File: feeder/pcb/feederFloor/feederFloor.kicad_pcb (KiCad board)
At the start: 2 copper layers, 13.5 x 40 mm, 6 parts, among them J1 Conn_01x04_Male, J2 Conn_01x10_Female, J3 Conn_01x04_Male

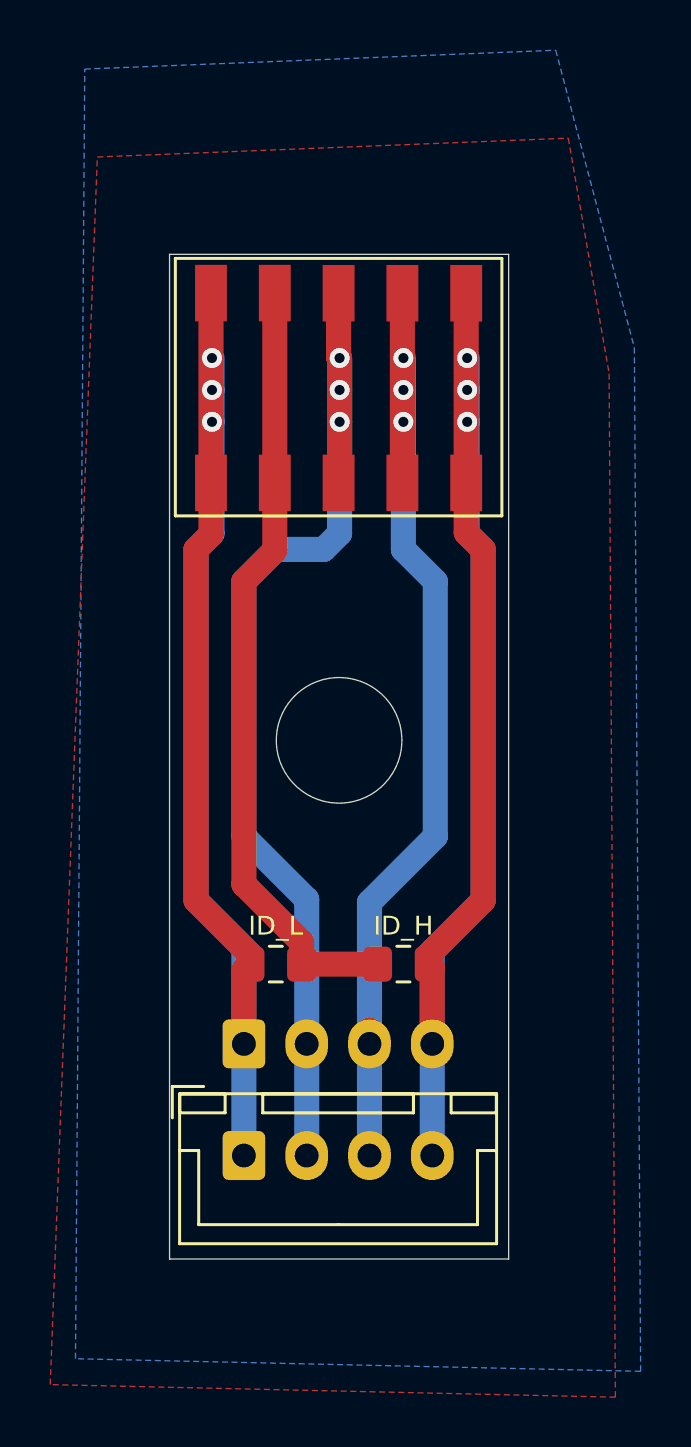
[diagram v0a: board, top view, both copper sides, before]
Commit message: this commit reflects boards ordered for rev04 of the feeder motherboard, rev02 of the indexing wheel, and rev02 of the feeder floor
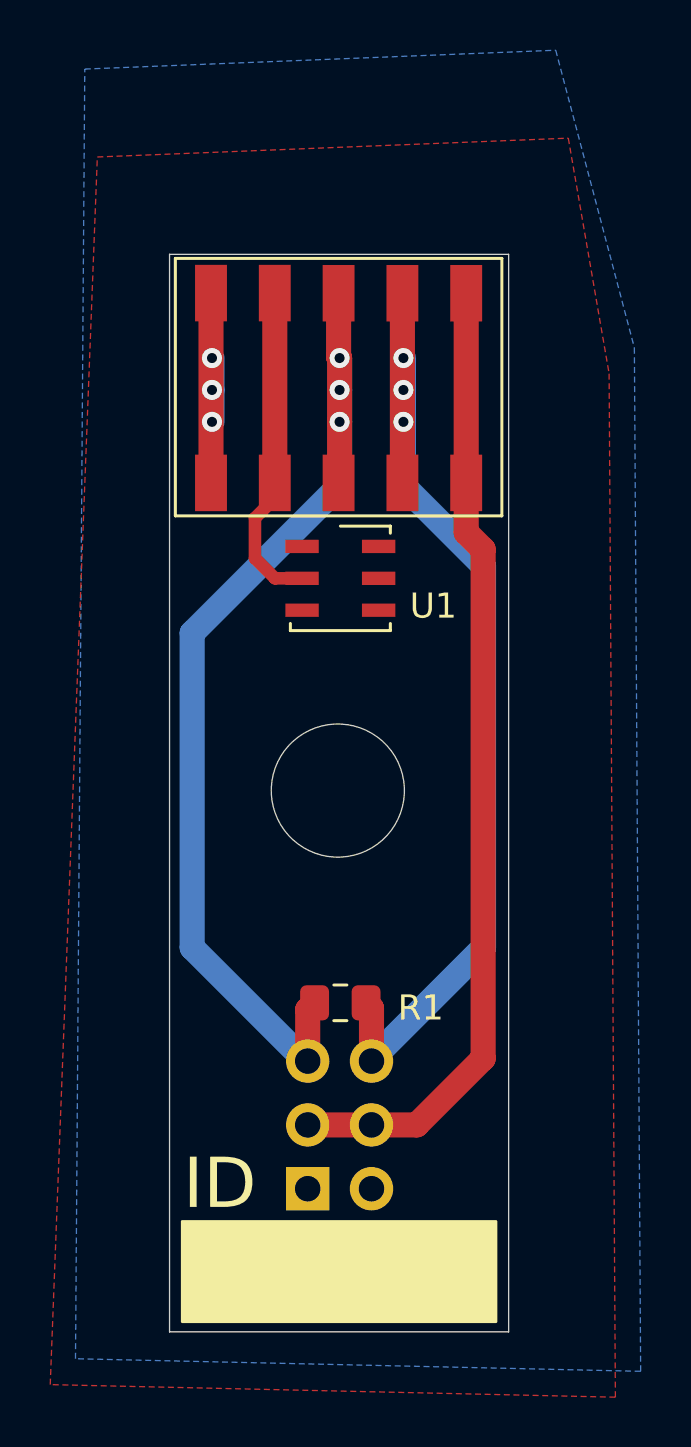
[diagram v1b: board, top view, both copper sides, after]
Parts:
- removed J3: Conn_01x04_Male, Connector_JST:JST_XH_B4B-XH-A_1x04_P2.50mm_Vertical
- removed R2: ID_L, Resistor_SMD:R_0805_2012Metric_Pad1.15x1.40mm_HandSolder
- added H1: MountingHole, MountingHole:MountingHole_5.3mm_M5, F.Cu at (191.7, 41.4)
- added U1: DS2431, Package_SO_J-Lead:TSOC-6_3.76x3.94mm_P1.27mm, F.Cu at (191.8, 32.9)
- J1: value Conn_01x04_Male -> IDC; footprint Connector_JST:JST_XH_B4B-XH-A_1x04_P2.50mm_Vertical -> Connector_IDC:IDC-Header_2x03_P2.54mm_Vertical
- R1: value ID_H -> 220R
- moved J1 6.30 mm to (190.5, 57.2)
- moved G*** 4.70 mm to (191.8, 25.4)
- moved R1 2.94 mm to (191.8, 49.8), turned to 0 degrees
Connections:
- J1 pad 2: B -> GND
- J1 pad 3: A -> VIN
- J1 pad 4: 5V -> VIN
- J2 pad 2: ID -> 1WIRE
- J2 pad 5: 5V -> VIN
- J2 pad 6: 5V -> VIN
- J2 pad 9: ID -> 1WIRE
- R1 pad 1: 5V -> B
- R1 pad 2: ID -> A
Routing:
- net 5V: track 64.0 -> 0.00 mm, vias 3 -> 0
- net GND: track 63.9 -> 10.1 mm
- net VIN: track 0.00 -> 38.8 mm
- net ID: track 31.2 -> 0.00 mm
- net 1WIRE: track 0.00 -> 13.2 mm
- net A: track 42.0 -> 41.1 mm
- net B: track 43.1 -> 42.4 mm
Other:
- board size 13.5 x 40 mm -> 13.5 x 42.9 mm
- board text added: "FEEDER FLOOR REV02"
- board text added: "ID"
- board text removed: "ID_H"
- board text removed: "ID_L"

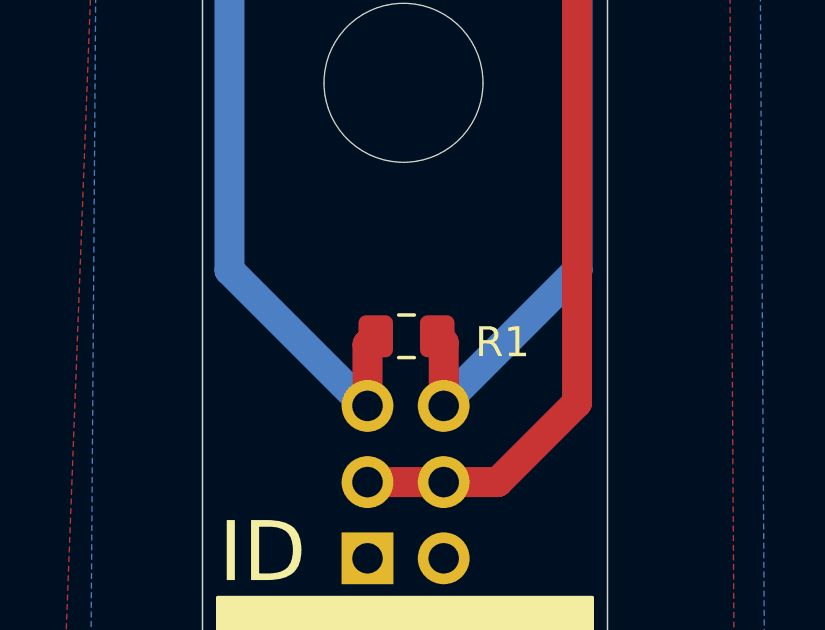
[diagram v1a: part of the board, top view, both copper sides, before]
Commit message: Updating the package of the resistor on the feeder floor.
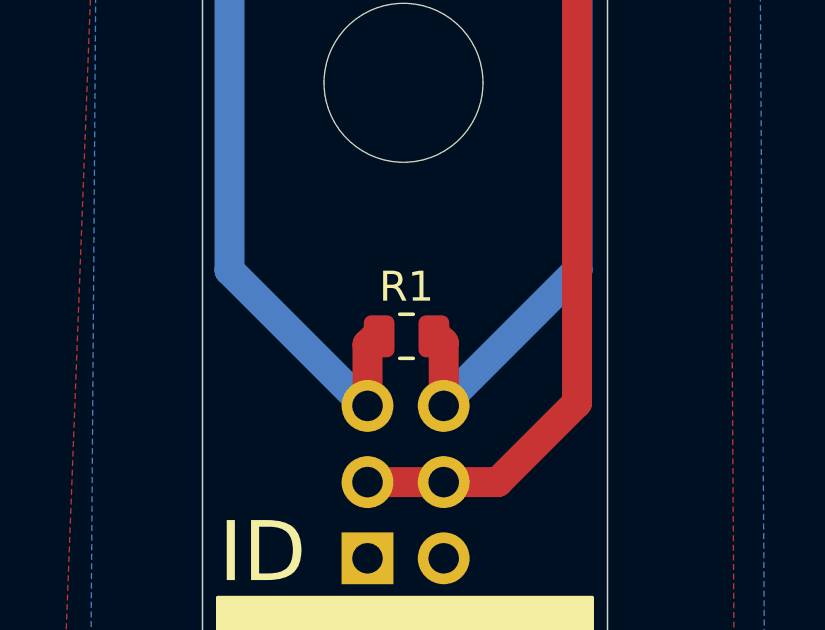
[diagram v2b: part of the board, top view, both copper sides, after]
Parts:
- R1: footprint Resistor_SMD:R_0805_2012Metric_Pad1.15x1.40mm_HandSolder -> Resistor_SMD:R_0805_2012Metric

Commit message: Adding the git hash to the feeder mobo, feeder floor and indexing wheel boards.
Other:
- board text added: "FEEDER FLOOR REV02 <<hash>>"
- board text removed: "FEEDER FLOOR REV02"

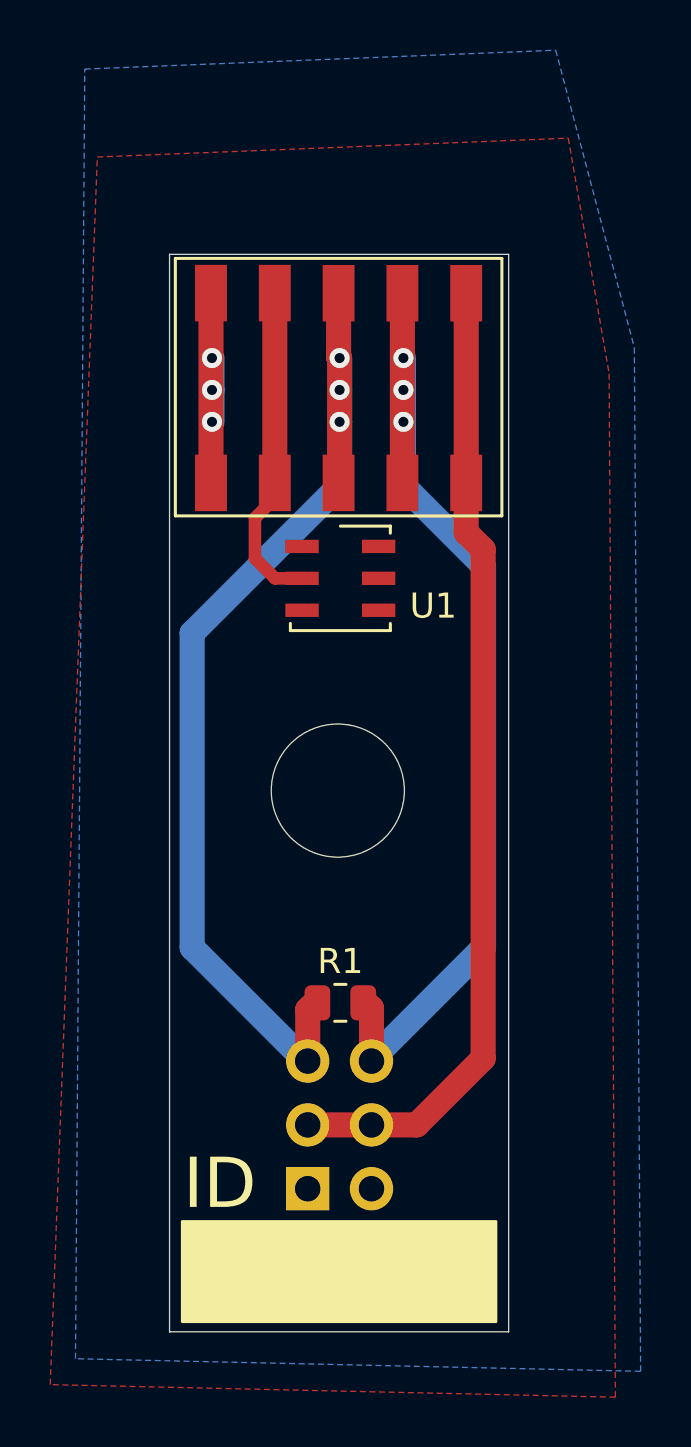
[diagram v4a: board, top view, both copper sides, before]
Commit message: Route bus as diff pairs, pad for screw head and beautify
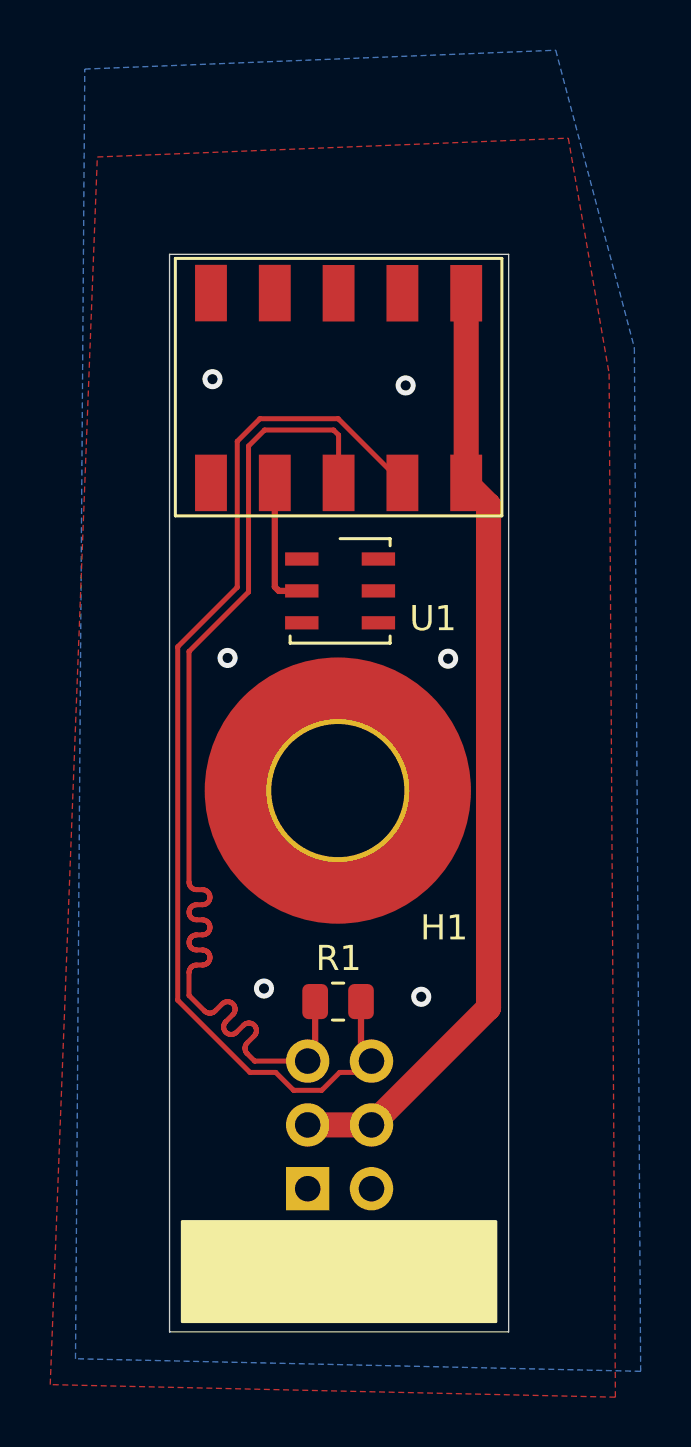
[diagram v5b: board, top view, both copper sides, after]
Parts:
- removed G***: LOGO, index:logo
- H1: footprint MountingHole:MountingHole_5.3mm_M5 -> MountingHole:MountingHole_5.3mm_M5_Pad_TopOnly
- R1: value 220R -> 120R
- moved U1 0.50 mm to (191.8, 33.4)
- moved R1 0.10 mm to (191.7, 49.8)
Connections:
- net A renamed RS-485+
- net B renamed RS-485-
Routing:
- net GND: track 10.1 -> 0.00 mm, vias 3 -> 6
- net 1WIRE: track 13.2 -> 5.28 mm
- net RS-485+: track 41.1 -> 43.5 mm, vias 3 -> 0
- net RS-485-: track 42.4 -> 43.4 mm, vias 3 -> 0
- net VIN: track 38.8 -> 37.9 mm
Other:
- board text removed: "ID"

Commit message: Fix bus wires on feeder floors
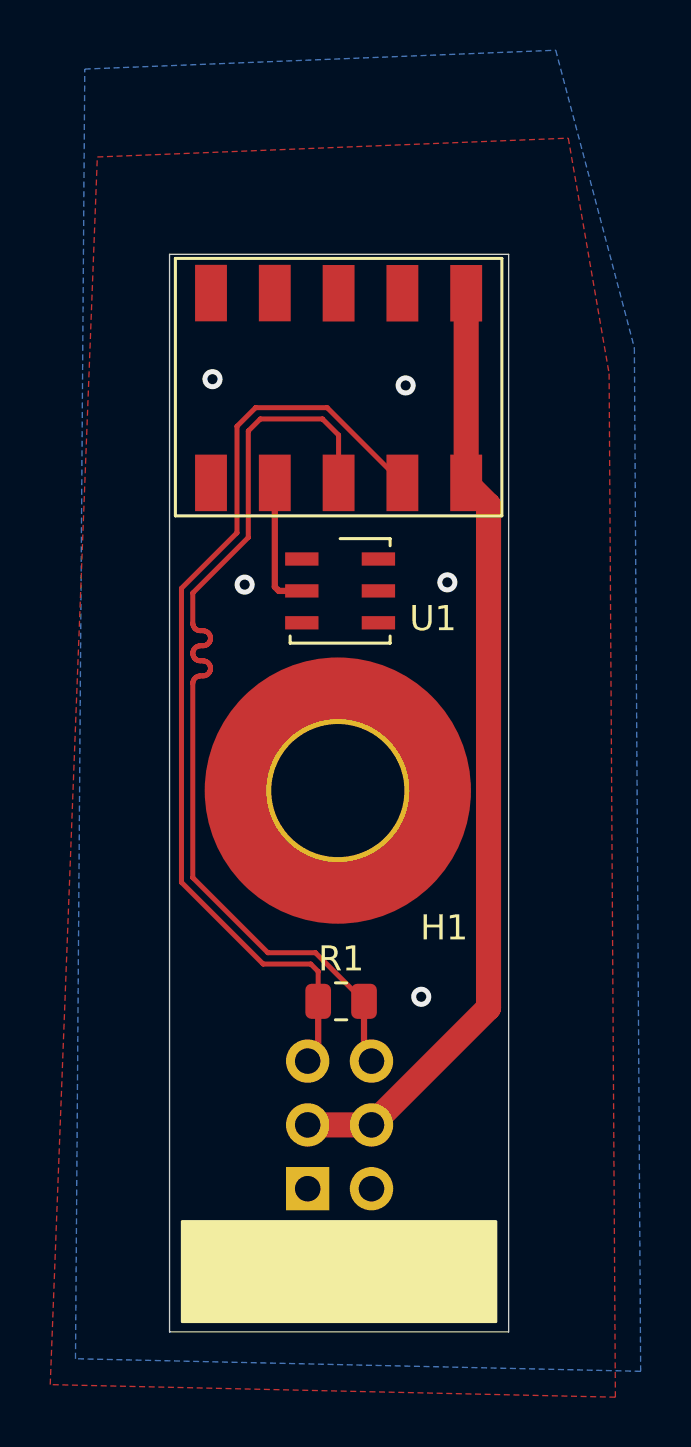
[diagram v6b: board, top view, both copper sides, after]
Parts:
- moved R1 0.12 mm to (191.8, 49.7), turned to 180 degrees
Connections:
- J1 pad 5: RS-485- -> RS-485+
- J1 pad 6: RS-485+ -> RS-485-
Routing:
- net RS-485-: track 43.4 -> 37.8 mm
- net RS-485+: track 43.5 -> 37.9 mm
- net GND: vias 6 -> 5

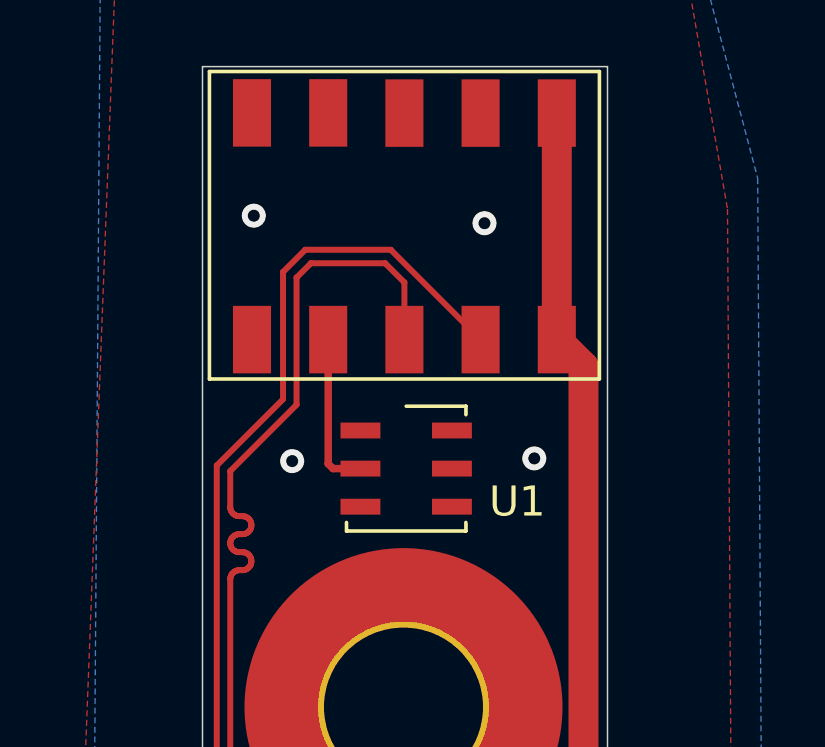
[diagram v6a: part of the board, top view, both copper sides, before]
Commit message: Add decorations to feeders
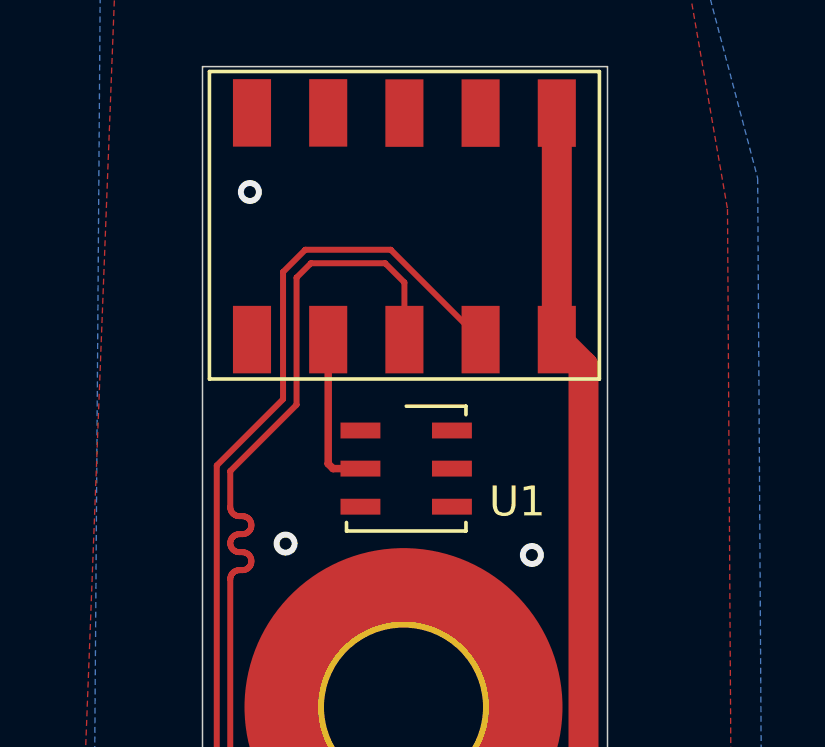
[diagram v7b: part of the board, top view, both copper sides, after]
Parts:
- added ?: , buzzard_labels, B.Cu at (191.8, 28.9)
- added ?: , buzzard_labels, B.Cu at (191.8, 26.4)
- added ?: , buzzard_labels, B.Cu at (191.7, 31.4)
- added ?: , buzzard_labels, B.Cu at (191.8, 23.8)
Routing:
- net GND: vias 5 -> 4
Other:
- board text added: "<<hash>>"
- board text removed: "FEEDER FLOOR REV02 <<hash>>"
